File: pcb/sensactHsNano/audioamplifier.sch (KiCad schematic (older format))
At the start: 25 parts, among them U1 TAS5805M

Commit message: Various PCB Updates
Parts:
- added J5: Conn_01x04, Connector_Phoenix_MC:PhoenixContact_MC_1,5_4-G-3.5_1x04_P3.50mm_Horizontal, symbol Connector_Generic:Conn_01x04
- C10, C11, C12, C13, C14, C2, C4, C5, C6, C7: footprint Capacitor_SMD:C_0805_2012Metric_Pad1.15x1.40mm_HandSolder -> Capacitor_SMD:C_0805_2012Metric_Pad1.18x1.45mm_HandSolder
- C15, C16, C17, C18: footprint Capacitor_SMD:C_0805_2012Metric_Pad1.15x1.40mm_HandSolder -> Capacitor_SMD:C_1206_3216Metric_Pad1.33x1.80mm_HandSolder
- C3, C9: value 1u -> 22u; footprint Capacitor_SMD:C_0805_2012Metric_Pad1.15x1.40mm_HandSolder -> Capacitor_SMD:C_1210_3225Metric_Pad1.33x2.70mm_HandSolder
- L1, L2: value 4u7 -> 10u/23mR; footprint smopla:L_0630 -> Inductor_SMD:L_Taiyo-Yuden_NR-10050_9.8x10.0mm_HandSoldering
- L3, L4: value 4u7 -> 10u; footprint smopla:L_0630 -> Inductor_SMD:L_Taiyo-Yuden_NR-10050_9.8x10.0mm_HandSoldering
- R2, R4: footprint Resistor_SMD:R_0805_2012Metric_Pad1.15x1.40mm_HandSolder -> Resistor_SMD:R_0805_2012Metric_Pad1.20x1.40mm_HandSolder
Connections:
- wire segments 72 -> 78
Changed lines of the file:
@@
 $Descr A4 11693 8268
 encoding utf-8
-Sheet 2 5
+Sheet 2 4
 Title ""
 Date ""
@@
 P 5250 2150
 F 0 "L1" V 5300 2300 50  0000 C CNN
-F 1 "4u7" V 5200 2150 50  0000 C CNN
-F 2 "smopla:L_0630" H 5250 2150 50  0001 C CNN
+F 1 "10u/23mR" V 5200 2150 50  0000 C CNN
+F 2 "Inductor_SMD:L_Taiyo-Yuden_NR-10050_9.8x10.0mm_HandSoldering" H 5250 2150 50  0001 C CNN
 F 3 "~" H 5250 2150 50  0001 C CNN
 	1    5250 2150
@@
 F 0 "C11" V 4900 1950 50  0000 C CNN
 F 1 "u22" V 4900 2200 50  0000 C CNN
-F 2 "Capacitor_SMD:C_0805_2012Metric_Pad1.15x1.40mm_HandSolder" H 4988 1900 50  0001 C CNN
+F 2 "Capacitor_SMD:C_0805_2012Metric_Pad1.18x1.45mm_HandSolder" H 4988 1900 50  0001 C CNN
 F 3 "~" H 4950 2050 50  0001 C CNN
 	1    4950 2050
@@
 P 5250 2250
 F 0 "L2" V 5300 2400 50  0000 C CNN
-F 1 "4u7" V 5350 2250 50  0000 C CNN
-F 2 "smopla:L_0630" H 5250 2250 50  0001 C CNN
+F 1 "10u/23mR" V 5350 2250 50  0000 C CNN
+F 2 "Inductor_SMD:L_Taiyo-Yuden_NR-10050_9.8x10.0mm_HandSoldering" H 5250 2250 50  0001 C CNN
 F 3 "~" H 5250 2250 50  0001 C CNN
 	1    5250 2250
@@
 F 0 "C12" V 5000 2250 50  0000 C CNN
 F 1 "u22" V 5000 2500 50  0000 C CNN
-F 2 "Capacitor_SMD:C_0805_2012Metric_Pad1.15x1.40mm_HandSolder" H 4988 2200 50  0001 C CNN
+F 2 "Capacitor_SMD:C_0805_2012Metric_Pad1.18x1.45mm_HandSolder" H 4988 2200 50  0001 C CNN
 F 3 "~" H 4950 2350 50  0001 C CNN
 	1    4950 2350
@@
 P 5250 2650
 F 0 "L3" V 5300 2800 50  0000 C CNN
-F 1 "4u7" V 5200 2650 50  0000 C CNN
-F 2 "smopla:L_0630" H 5250 2650 50  0001 C CNN
+F 1 "10u" V 5200 2650 50  0000 C CNN
+F 2 "Inductor_SMD:L_Taiyo-Yuden_NR-10050_9.8x10.0mm_HandSoldering" H 5250 2650 50  0001 C CNN
 F 3 "~" H 5250 2650 50  0001 C CNN
 	1    5250 2650
@@
 F 0 "C13" V 4900 2450 50  0000 C CNN
 F 1 "u22" V 4900 2700 50  0000 C CNN
-F 2 "Capacitor_SMD:C_0805_2012Metric_Pad1.15x1.40mm_HandSolder" H 4988 2400 50  0001 C CNN
+F 2 "Capacitor_SMD:C_0805_2012Metric_Pad1.18x1.45mm_HandSolder" H 4988 2400 50  0001 C CNN
 F 3 "~" H 4950 2550 50  0001 C CNN
 	1    4950 2550
@@
 P 5250 2750
 F 0 "L4" V 5300 2900 50  0000 C CNN
-F 1 "4u7" V 5350 2750 50  0000 C CNN
-F 2 "smopla:L_0630" H 5250 2750 50  0001 C CNN
+F 1 "10u" V 5350 2750 50  0000 C CNN
+F 2 "Inductor_SMD:L_Taiyo-Yuden_NR-10050_9.8x10.0mm_HandSoldering" H 5250 2750 50  0001 C CNN
 F 3 "~" H 5250 2750 50  0001 C CNN
 	1    5250 2750
@@
 F 0 "C14" V 5000 2750 50  0000 C CNN
 F 1 "u22" V 5000 3000 50  0000 C CNN
-F 2 "Capacitor_SMD:C_0805_2012Metric_Pad1.15x1.40mm_HandSolder" H 4988 2700 50  0001 C CNN
+F 2 "Capacitor_SMD:C_0805_2012Metric_Pad1.18x1.45mm_HandSolder" H 4988 2700 50  0001 C CNN
 F 3 "~" H 4950 2850 50  0001 C CNN
 	1    4950 2850
@@
 F 0 "C15" H 5650 2300 50  0000 C CNN
 F 1 "u68" H 5700 2500 50  0000 C CNN
-F 2 "Capacitor_SMD:C_0805_2012Metric_Pad1.15x1.40mm_HandSolder" H 5638 2250 50  0001 C CNN
+F 2 "Capacitor_SMD:C_1206_3216Metric_Pad1.33x1.80mm_HandSolder" H 5638 2250 50  0001 C CNN
 F 3 "~" H 5600 2400 50  0001 C CNN
 	1    5600 2400
@@
 F 0 "C17" H 5950 2300 50  0000 C CNN
 F 1 "u68" H 6000 2500 50  0000 C CNN
-F 2 "Capacitor_SMD:C_0805_2012Metric_Pad1.15x1.40mm_HandSolder" H 5938 2250 50  0001 C CNN
+F 2 "Capacitor_SMD:C_1206_3216Metric_Pad1.33x1.80mm_HandSolder" H 5938 2250 50  0001 C CNN
 F 3 "~" H 5900 2400 50  0001 C CNN
 	1    5900 2400
@@
 Wire Wire Line
 	5900 2150 5900 2250
-Wire Wire Line
-	5900 2150 6400 2150
 Connection ~ 5900 2150
 Text Label 6150 2150 0    50   ~ 0
@@
 F 0 "C16" H 5650 2800 50  0000 C CNN
 F 1 "u68" H 5700 3000 50  0000 C CNN
-F 2 "Capacitor_SMD:C_0805_2012Metric_Pad1.15x1.40mm_HandSolder" H 5638 2750 50  0001 C CNN
+F 2 "Capacitor_SMD:C_1206_3216Metric_Pad1.33x1.80mm_HandSolder" H 5638 2750 50  0001 C CNN
 F 3 "~" H 5600 2900 50  0001 C CNN
 	1    5600 2900
@@
 F 0 "C18" H 5950 2800 50  0000 C CNN
 F 1 "u68" H 6000 3000 50  0000 C CNN
-F 2 "Capacitor_SMD:C_0805_2012Metric_Pad1.15x1.40mm_HandSolder" H 5938 2750 50  0001 C CNN
+F 2 "Capacitor_SMD:C_1206_3216Metric_Pad1.33x1.80mm_HandSolder" H 5938 2750 50  0001 C CNN
 F 3 "~" H 5900 2900 50  0001 C CNN
 	1    5900 2900
@@
 Wire Wire Line
 	5950 2700 5950 2750
-Wire Wire Line
-	5950 2750 6400 2750
 Connection ~ 5600 2750
 Wire Wire Line
@@
 Wire Wire Line
 	5900 2650 5900 2750
-Wire Wire Line
-	5900 2650 6400 2650
 Connection ~ 5900 2650
 Text Label 6150 2650 0    50   ~ 0
@@
 P 3150 1550
 F 0 "C3" H 3265 1596 50  0000 L CNN
-F 1 "1u" H 3265 1505 50  0000 L CNN
-F 2 "Capacitor_SMD:C_0805_2012Metric_Pad1.15x1.40mm_HandSolder" H 3188 1400 50  0001 C CNN
+F 1 "22u" H 3265 1505 50  0000 L CNN
+F 2 "Capacitor_SMD:C_1210_3225Metric_Pad1.33x2.70mm_HandSolder" H 3188 1400 50  0001 C CNN
 F 3 "~" H 3150 1550 50  0001 C CNN
 	1    3150 1550
@@
 F 0 "C5" H 3565 1596 50  0000 L CNN
 F 1 "u1" H 3565 1505 50  0000 L CNN
-F 2 "Capacitor_SMD:C_0805_2012Metric_Pad1.15x1.40mm_HandSolder" H 3488 1400 50  0001 C CNN
+F 2 "Capacitor_SMD:C_0805_2012Metric_Pad1.18x1.45mm_HandSolder" H 3488 1400 50  0001 C CNN
 F 3 "~" H 3450 1550 50  0001 C CNN
 	1    3450 1550
@@
 P 4300 1550
 F 0 "C9" H 4415 1596 50  0000 L CNN
-F 1 "1u" H 4415 1505 50  0000 L CNN
-F 2 "Capacitor_SMD:C_0805_2012Metric_Pad1.15x1.40mm_HandSolder" H 4338 1400 50  0001 C CNN
+F 1 "22u" H 4415 1505 50  0000 L CNN
+F 2 "Capacitor_SMD:C_1210_3225Metric_Pad1.33x2.70mm_HandSolder" H 4338 1400 50  0001 C CNN
 F 3 "~" H 4300 1550 50  0001 C CNN
 	1    4300 1550
@@
 F 0 "C10" H 4715 1596 50  0000 L CNN
 F 1 "u1" H 4715 1505 50  0000 L CNN
-F 2 "Capacitor_SMD:C_0805_2012Metric_Pad1.15x1.40mm_HandSolder" H 4638 1400 50  0001 C CNN
+F 2 "Capacitor_SMD:C_0805_2012Metric_Pad1.18x1.45mm_HandSolder" H 4638 1400 50  0001 C CNN
 F 3 "~" H 4600 1550 50  0001 C CNN
 	1    4600 1550
@@
 F 0 "C2" H 3215 2346 50  0000 L CNN
 F 1 "1u" H 3215 2255 50  0000 L CNN
-F 2 "Capacitor_SMD:C_0805_2012Metric_Pad1.15x1.40mm_HandSolder" H 3138 2150 50  0001 C CNN
+F 2 "Capacitor_SMD:C_0805_2012Metric_Pad1.18x1.45mm_HandSolder" H 3138 2150 50  0001 C CNN
 F 3 "~" H 3100 2300 50  0001 C CNN
 	1    3100 2300
@@
 F 0 "C4" H 3515 2346 50  0000 L CNN
 F 1 "u1" H 3515 2255 50  0000 L CNN
-F 2 "Capacitor_SMD:C_0805_2012Metric_Pad1.15x1.40mm_HandSolder" H 3438 2150 50  0001 C CNN
+F 2 "Capacitor_SMD:C_0805_2012Metric_Pad1.18x1.45mm_HandSolder" H 3438 2150 50  0001 C CNN
 F 3 "~" H 3400 2300 50  0001 C CNN
 	1    3400 2300
@@
 F 0 "C6" V 3450 2600 50  0000 C CNN
 F 1 "1u" V 3450 2800 50  0000 C CNN
-F 2 "Capacitor_SMD:C_0805_2012Metric_Pad1.15x1.40mm_HandSolder" H 3538 2550 50  0001 C CNN
+F 2 "Capacitor_SMD:C_0805_2012Metric_Pad1.18x1.45mm_HandSolder" H 3538 2550 50  0001 C CNN
 F 3 "~" H 3500 2700 50  0001 C CNN
 	1    3500 2700
@@
 F 0 "C7" V 3450 2800 50  0000 C CNN
 F 1 "1u" V 3450 3000 50  0000 C CNN
-F 2 "Capacitor_SMD:C_0805_2012Metric_Pad1.15x1.40mm_HandSolder" H 3538 2750 50  0001 C CNN
+F 2 "Capacitor_SMD:C_0805_2012Metric_Pad1.18x1.45mm_HandSolder" H 3538 2750 50  0001 C CNN
 F 3 "~" H 3500 2900 50  0001 C CNN
 	1    3500 2900
@@
 F 0 "R2" H 2620 3596 50  0000 L CNN
 F 1 "4k7" H 2620 3505 50  0000 L CNN
-F 2 "Resistor_SMD:R_0805_2012Metric_Pad1.15x1.40mm_HandSolder" V 2480 3550 50  0001 C CNN
+F 2 "Resistor_SMD:R_0805_2012Metric_Pad1.20x1.40mm_HandSolder" V 2480 3550 50  0001 C CNN
 F 3 "~" H 2550 3550 50  0001 C CNN
 	1    2550 3550
@@
 F 0 "R4" H 2920 3596 50  0000 L CNN
 F 1 "4k7" H 2920 3505 50  0000 L CNN
-F 2 "Resistor_SMD:R_0805_2012Metric_Pad1.15x1.40mm_HandSolder" V 2780 3550 50  0001 C CNN
+F 2 "Resistor_SMD:R_0805_2012Metric_Pad1.20x1.40mm_HandSolder" V 2780 3550 50  0001 C CNN
 F 3 "~" H 2850 3550 50  0001 C CNN
 	1    2850 3550
@@
 Text GLabel 3800 3850 0    50   BiDi ~ 0
 SDIN
+$Comp
+L Connector_Generic:Conn_01x04 J5
+U 1 1 60EF2319
+P 6700 2500
+F 0 "J5" H 6618 2075 50  0000 C CNN
+F 1 "Conn_01x04" H 6618 2166 50  0000 C CNN
+F 2 "Connector_Phoenix_MC:PhoenixContact_MC_1,5_4-G-3.5_1x04_P3.50mm_Horizontal" H 6700 2500 50  0001 C CNN
+F 3 "~" H 6700 2500 50  0001 C CNN
+	1    6700 2500
+	1    0    0    1
+$EndComp
+Wire Wire Line
+	6400 2250 6400 2400
+Wire Wire Line
+	6400 2400 6500 2400
+Wire Wire Line
+	5950 2750 6450 2750
+Wire Wire Line
+	5900 2150 6500 2150
+Wire Wire Line
+	6500 2650 6500 2600
+Wire Wire Line
+	5900 2650 6500 2650
+Wire Wire Line
+	6450 2750 6450 2500
+Wire Wire Line
+	6450 2500 6500 2500
+Wire Wire Line
+	6500 2150 6500 2300
 $EndSCHEMATC

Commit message: Updated sensactHsNano
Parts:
- C1, C8: footprint Capacitor_SMD:CP_Elec_10x10.5 -> Capacitor_THT:CP_Radial_D10.0mm_P3.50mm
- C3, C9: footprint Capacitor_SMD:C_1210_3225Metric_Pad1.33x2.70mm_HandSolder -> Capacitor_SMD:C_1206_3216Metric_Pad1.33x1.80mm_HandSolder
- J5: value Conn_01x04 -> Audio
- L1, L2: value 10u/23mR -> 10u; footprint Inductor_SMD:L_Taiyo-Yuden_NR-10050_9.8x10.0mm_HandSoldering -> liebler_PASSIVES:Inductor_CDRH104_handsolder
- L3, L4: footprint Inductor_SMD:L_Taiyo-Yuden_NR-10050_9.8x10.0mm_HandSoldering -> liebler_PASSIVES:Inductor_CDRH104_handsolder
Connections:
- net labels added: AMP_PDN, SCL2, SDA2
- net labels removed: SCL1, SDA1
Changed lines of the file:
@@
 P 5250 2150
 F 0 "L1" V 5300 2300 50  0000 C CNN
-F 1 "10u/23mR" V 5200 2150 50  0000 C CNN
-F 2 "Inductor_SMD:L_Taiyo-Yuden_NR-10050_9.8x10.0mm_HandSoldering" H 5250 2150 50  0001 C CNN
+F 1 "10u" V 5200 2150 50  0000 C CNN
+F 2 "liebler_PASSIVES:Inductor_CDRH104_handsolder" H 5250 2150 50  0001 C CNN
 F 3 "~" H 5250 2150 50  0001 C CNN
 	1    5250 2150
@@
 P 5250 2250
 F 0 "L2" V 5300 2400 50  0000 C CNN
-F 1 "10u/23mR" V 5350 2250 50  0000 C CNN
-F 2 "Inductor_SMD:L_Taiyo-Yuden_NR-10050_9.8x10.0mm_HandSoldering" H 5250 2250 50  0001 C CNN
+F 1 "10u" V 5350 2250 50  0000 C CNN
+F 2 "liebler_PASSIVES:Inductor_CDRH104_handsolder" H 5250 2250 50  0001 C CNN
 F 3 "~" H 5250 2250 50  0001 C CNN
 	1    5250 2250
@@
 F 0 "L3" V 5300 2800 50  0000 C CNN
 F 1 "10u" V 5200 2650 50  0000 C CNN
-F 2 "Inductor_SMD:L_Taiyo-Yuden_NR-10050_9.8x10.0mm_HandSoldering" H 5250 2650 50  0001 C CNN
+F 2 "liebler_PASSIVES:Inductor_CDRH104_handsolder" H 5250 2650 50  0001 C CNN
 F 3 "~" H 5250 2650 50  0001 C CNN
 	1    5250 2650
@@
 F 0 "L4" V 5300 2900 50  0000 C CNN
 F 1 "10u" V 5350 2750 50  0000 C CNN
-F 2 "Inductor_SMD:L_Taiyo-Yuden_NR-10050_9.8x10.0mm_HandSoldering" H 5250 2750 50  0001 C CNN
+F 2 "liebler_PASSIVES:Inductor_CDRH104_handsolder" H 5250 2750 50  0001 C CNN
 F 3 "~" H 5250 2750 50  0001 C CNN
 	1    5250 2750
@@
 F 0 "C3" H 3265 1596 50  0000 L CNN
 F 1 "22u" H 3265 1505 50  0000 L CNN
-F 2 "Capacitor_SMD:C_1210_3225Metric_Pad1.33x2.70mm_HandSolder" H 3188 1400 50  0001 C CNN
+F 2 "Capacitor_SMD:C_1206_3216Metric_Pad1.33x1.80mm_HandSolder" H 3188 1400 50  0001 C CNN
 F 3 "~" H 3150 1550 50  0001 C CNN
 	1    3150 1550
@@
 F 0 "C1" H 2918 1596 50  0000 L CNN
 F 1 "470u" H 2918 1505 50  0000 L CNN
-F 2 "Capacitor_SMD:CP_Elec_10x10.5" H 2838 1400 50  0001 C CNN
+F 2 "Capacitor_THT:CP_Radial_D10.0mm_P3.50mm" H 2838 1400 50  0001 C CNN
 F 3 "~" H 2800 1550 50  0001 C CNN
 	1    2800 1550
@@
 F 0 "C9" H 4415 1596 50  0000 L CNN
 F 1 "22u" H 4415 1505 50  0000 L CNN
-F 2 "Capacitor_SMD:C_1210_3225Metric_Pad1.33x2.70mm_HandSolder" H 4338 1400 50  0001 C CNN
+F 2 "Capacitor_SMD:C_1206_3216Metric_Pad1.33x1.80mm_HandSolder" H 4338 1400 50  0001 C CNN
 F 3 "~" H 4300 1550 50  0001 C CNN
 	1    4300 1550
@@
 F 0 "C8" H 4068 1596 50  0000 L CNN
 F 1 "470u" H 4068 1505 50  0000 L CNN
-F 2 "Capacitor_SMD:CP_Elec_10x10.5" H 3988 1400 50  0001 C CNN
+F 2 "Capacitor_THT:CP_Radial_D10.0mm_P3.50mm" H 3988 1400 50  0001 C CNN
 F 3 "~" H 3950 1550 50  0001 C CNN
 	1    3950 1550
@@
 	2250 3150 3800 3150
 Text GLabel 2250 3050 0    50   BiDi ~ 0
-SDA1
+SDA2
 Text GLabel 2250 3150 0    50   BiDi ~ 0
-SCL1
+SCL2
 Text GLabel 3800 3750 0    50   BiDi ~ 0
 SCLK
@@
 P 6700 2500
 F 0 "J5" H 6618 2075 50  0000 C CNN
-F 1 "Conn_01x04" H 6618 2166 50  0000 C CNN
+F 1 "Audio" H 6618 2166 50  0000 C CNN
 F 2 "Connector_Phoenix_MC:PhoenixContact_MC_1,5_4-G-3.5_1x04_P3.50mm_Horizontal" H 6700 2500 50  0001 C CNN
 F 3 "~" H 6700 2500 50  0001 C CNN
@@
 Wire Wire Line
 	6500 2150 6500 2300
+Text GLabel 2300 3850 0    50   Input ~ 0
+AMP_PDN
 $EndSCHEMATC

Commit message: Complete reorganisation
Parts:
- removed J5: Audio, Connector_Phoenix_MC:PhoenixContact_MC_1,5_4-G-3.5_1x04_P3.50mm_Horizontal, symbol Connector_Generic:Conn_01x04
- U1: symbol sensact:TAS5805M -> sensactHsNano-rescue:TAS5805M-sensact
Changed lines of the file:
@@
 $Descr A4 11693 8268
 encoding utf-8
-Sheet 2 4
+Sheet 2 5
 Title ""
 Date ""
@@
 $EndComp
 $Comp
-L sensact:TAS5805M U1
+L sensactHsNano-rescue:TAS5805M-sensact U1
 U 1 1 5F9CF512
 P 4300 2950
@@
 Text GLabel 3800 3850 0    50   BiDi ~ 0
 SDIN
-$Comp
-L Connector_Generic:Conn_01x04 J5
-U 1 1 60EF2319
-P 6700 2500
-F 0 "J5" H 6618 2075 50  0000 C CNN
-F 1 "Audio" H 6618 2166 50  0000 C CNN
-F 2 "Connector_Phoenix_MC:PhoenixContact_MC_1,5_4-G-3.5_1x04_P3.50mm_Horizontal" H 6700 2500 50  0001 C CNN
-F 3 "~" H 6700 2500 50  0001 C CNN
-	1    6700 2500
-	1    0    0    1
-$EndComp
 Wire Wire Line
 	6400 2250 6400 2400
@@
 Wire Wire Line
 	5950 2750 6450 2750
-Wire Wire Line
-	5900 2150 6500 2150
 Wire Wire Line
 	6500 2650 6500 2600
@@
 Text GLabel 2300 3850 0    50   Input ~ 0
 AMP_PDN
+Wire Wire Line
+	5900 2150 6500 2150
+Text GLabel 6500 2300 2    50   BiDi ~ 0
+OUT_A+
+Text GLabel 6500 2400 2    50   BiDi ~ 0
+OUT_A-
+Text GLabel 6500 2500 2    50   BiDi ~ 0
+OUT_B-
+Text GLabel 6500 2600 2    50   BiDi ~ 0
+OUT_B+
 $EndSCHEMATC

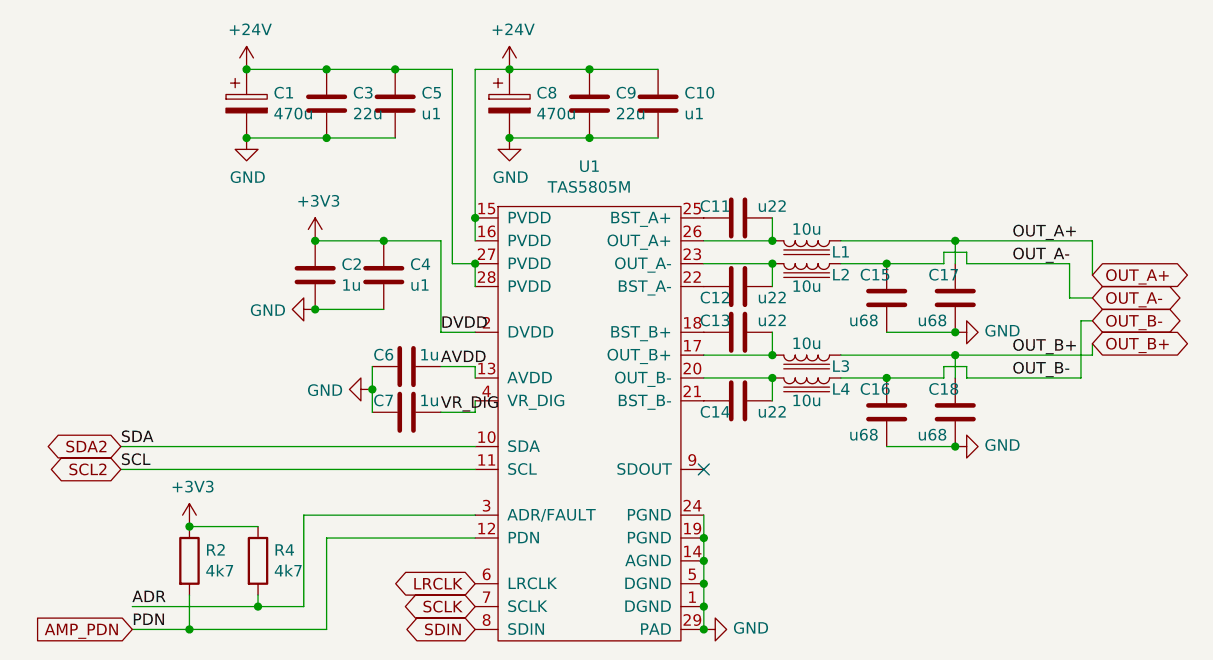
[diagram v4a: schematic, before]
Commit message: sensactUP2, sensactHsNano sensactHsLED sensactOutdoor as ordered at JLCPCB
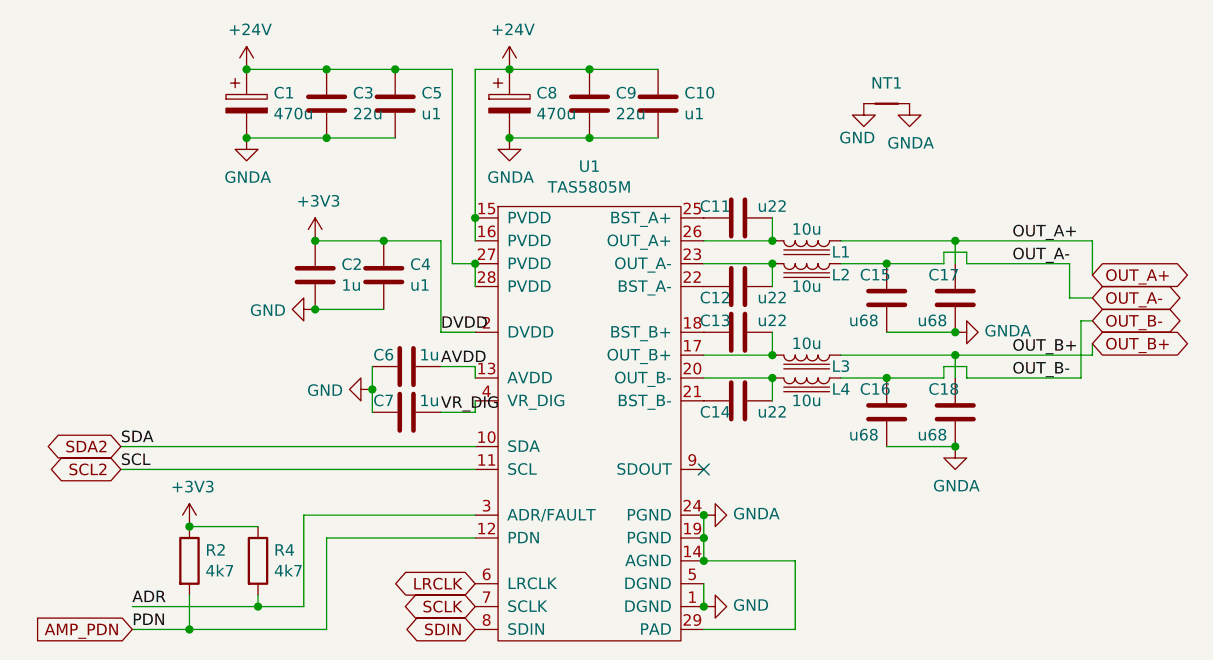
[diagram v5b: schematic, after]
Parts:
- added NT1: Net-Tie_2, NetTie:NetTie-2_SMD_Pad2.0mm, symbol Device:Net-Tie_2
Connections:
- net GND: now also NT1.1; no longer C1.2, C10.2, C15.1, C16.1, C17.1, C18.1, C3.2, C5.2, C8.2, C9.2, U1.14 (AGND), U1.19 (PGND), U1.24 (PGND), U1.29 (PAD)
- new net GNDA: C1.2, C10.2, C15.1, C16.1, C17.1, C18.1, C3.2, C5.2, C8.2, C9.2, NT1.2, U1.14 (AGND), U1.19 (PGND), U1.24 (PGND), U1.29 (PAD)
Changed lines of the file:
@@
 	5600 3050 5900 3050
 NoConn ~ 4800 3150
-Wire Wire Line
-	4800 3850 4800 3750
-Connection ~ 4800 3450
-Wire Wire Line
-	4800 3450 4800 3350
-Connection ~ 4800 3550
-Wire Wire Line
-	4800 3550 4800 3450
-Connection ~ 4800 3650
-Wire Wire Line
-	4800 3650 4800 3550
 Connection ~ 4800 3750
 Wire Wire Line
@@
 	1    0    0    -1
 $EndComp
-$Comp
-L power:GND #PWR04
-U 1 1 5F9DE396
-P 2800 1700
-F 0 "#PWR04" H 2800 1450 50  0001 C CNN
-F 1 "GND" H 2805 1527 50  0000 C CNN
-F 2 "" H 2800 1700 50  0001 C CNN
-F 3 "" H 2800 1700 50  0001 C CNN
-	1    2800 1700
-	1    0    0    -1
-$EndComp
-$Comp
-L power:GND #PWR011
-U 1 1 5F9DE9A3
-P 5900 2550
-F 0 "#PWR011" H 5900 2300 50  0001 C CNN
-F 1 "GND" V 5905 2422 50  0000 R CNN
-F 2 "" H 5900 2550 50  0001 C CNN
-F 3 "" H 5900 2550 50  0001 C CNN
-	1    5900 2550
-	0    -1   -1   0
-$EndComp
-Connection ~ 5900 2550
-$Comp
-L power:GND #PWR012
-U 1 1 5F9DF724
-P 5900 3050
-F 0 "#PWR012" H 5900 2800 50  0001 C CNN
-F 1 "GND" V 5905 2922 50  0000 R CNN
-F 2 "" H 5900 3050 50  0001 C CNN
-F 3 "" H 5900 3050 50  0001 C CNN
-	1    5900 3050
-	0    -1   -1   0
-$EndComp
 Connection ~ 5900 3050
 $Comp
 L power:GND #PWR010
 U 1 1 5F9DFBFC
-P 4800 3850
-F 0 "#PWR010" H 4800 3600 50  0001 C CNN
-F 1 "GND" V 4805 3722 50  0000 R CNN
-F 2 "" H 4800 3850 50  0001 C CNN
-F 3 "" H 4800 3850 50  0001 C CNN
-	1    4800 3850
+P 4800 3750
+F 0 "#PWR010" H 4800 3500 50  0001 C CNN
+F 1 "GND" V 4805 3622 50  0000 R CNN
+F 2 "" H 4800 3750 50  0001 C CNN
+F 3 "" H 4800 3750 50  0001 C CNN
+	1    4800 3750
 	0    -1   -1   0
 $EndComp
-Connection ~ 4800 3850
 $Comp
 L Device:C C9
@@
 	1    0    0    -1
 $EndComp
-$Comp
-L power:GND #PWR09
-U 1 1 5F9E0233
-P 3950 1700
-F 0 "#PWR09" H 3950 1450 50  0001 C CNN
-F 1 "GND" H 3955 1527 50  0000 C CNN
-F 2 "" H 3950 1700 50  0001 C CNN
-F 3 "" H 3950 1700 50  0001 C CNN
-	1    3950 1700
-	1    0    0    -1
-$EndComp
 Wire Wire Line
 	3450 1400 3150 1400
@@
 Wire Wire Line
 	3450 1700 3150 1700
-Connection ~ 2800 1700
 Connection ~ 3150 1700
 Wire Wire Line
@@
 Wire Wire Line
 	4600 1700 4300 1700
-Connection ~ 3950 1700
 Connection ~ 4300 1700
 Wire Wire Line
@@
 Text GLabel 6500 2600 2    50   BiDi ~ 0
 OUT_B+
+$Comp
+L power:GNDA #PWR059
+U 1 1 60FFE1B5
+P 5900 3050
+F 0 "#PWR059" H 5900 2800 50  0001 C CNN
+F 1 "GNDA" H 5905 2877 50  0000 C CNN
+F 2 "" H 5900 3050 50  0001 C CNN
+F 3 "" H 5900 3050 50  0001 C CNN
+	1    5900 3050
+	1    0    0    -1
+$EndComp
+$Comp
+L power:GNDA #PWR011
+U 1 1 60FFE78F
+P 4800 3350
+F 0 "#PWR011" H 4800 3100 50  0001 C CNN
+F 1 "GNDA" V 4805 3222 50  0000 R CNN
+F 2 "" H 4800 3350 50  0001 C CNN
+F 3 "" H 4800 3350 50  0001 C CNN
+	1    4800 3350
+	0    -1   -1   0
+$EndComp
+Wire Wire Line
+	4800 3550 4800 3450
+Connection ~ 4800 3350
+Connection ~ 4800 3450
+Wire Wire Line
+	4800 3450 4800 3350
+$Comp
+L power:GNDA #PWR058
+U 1 1 61000EDD
+P 5900 2550
+F 0 "#PWR058" H 5900 2300 50  0001 C CNN
+F 1 "GNDA" V 5905 2422 50  0000 R CNN
+F 2 "" H 5900 2550 50  0001 C CNN
+F 3 "" H 5900 2550 50  0001 C CNN
+	1    5900 2550
+	0    -1   -1   0
+$EndComp
+Connection ~ 5900 2550
+$Comp
+L power:GNDA #PWR09
+U 1 1 610016F9
+P 3950 1700
+F 0 "#PWR09" H 3950 1450 50  0001 C CNN
+F 1 "GNDA" H 3955 1527 50  0000 C CNN
+F 2 "" H 3950 1700 50  0001 C CNN
+F 3 "" H 3950 1700 50  0001 C CNN
+	1    3950 1700
+	1    0    0    -1
+$EndComp
+Connection ~ 3950 1700
+$Comp
+L power:GNDA #PWR04
+U 1 1 61001C29
+P 2800 1700
+F 0 "#PWR04" H 2800 1450 50  0001 C CNN
+F 1 "GNDA" H 2805 1527 50  0000 C CNN
+F 2 "" H 2800 1700 50  0001 C CNN
+F 3 "" H 2800 1700 50  0001 C CNN
+	1    2800 1700
+	1    0    0    -1
+$EndComp
+Connection ~ 2800 1700
+$Comp
+L Device:Net-Tie_2 NT1
+U 1 1 610023A8
+P 5600 1550
+F 0 "NT1" H 5600 1639 50  0000 C CNN
+F 1 "Net-Tie_2" H 5600 1640 50  0001 C CNN
+F 2 "NetTie:NetTie-2_SMD_Pad2.0mm" H 5600 1550 50  0001 C CNN
+F 3 "~" H 5600 1550 50  0001 C CNN
+	1    5600 1550
+	1    0    0    -1
+$EndComp
+$Comp
+L power:GNDA #PWR057
+U 1 1 61002769
+P 5700 1550
+F 0 "#PWR057" H 5700 1300 50  0001 C CNN
+F 1 "GNDA" H 5705 1377 50  0000 C CNN
+F 2 "" H 5700 1550 50  0001 C CNN
+F 3 "" H 5700 1550 50  0001 C CNN
+	1    5700 1550
+	1    0    0    -1
+$EndComp
+$Comp
+L power:GND #PWR012
+U 1 1 61002C22
+P 5500 1550
+F 0 "#PWR012" H 5500 1300 50  0001 C CNN
+F 1 "GND" H 5550 1400 50  0000 R CNN
+F 2 "" H 5500 1550 50  0001 C CNN
+F 3 "" H 5500 1550 50  0001 C CNN
+	1    5500 1550
+	1    0    0    -1
+$EndComp
+Wire Wire Line
+	4800 3850 5200 3850
+Wire Wire Line
+	5200 3850 5200 3550
+Wire Wire Line
+	5200 3550 4800 3550
+Connection ~ 4800 3550
 $EndSCHEMATC
